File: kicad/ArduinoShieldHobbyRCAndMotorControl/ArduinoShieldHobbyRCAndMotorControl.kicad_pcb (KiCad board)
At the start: 2 copper layers, 68.6 x 53.3 mm, 18 parts, among them J1 Power, J2 Digital/PWM, J3 Analog, J4 Digital/PWM

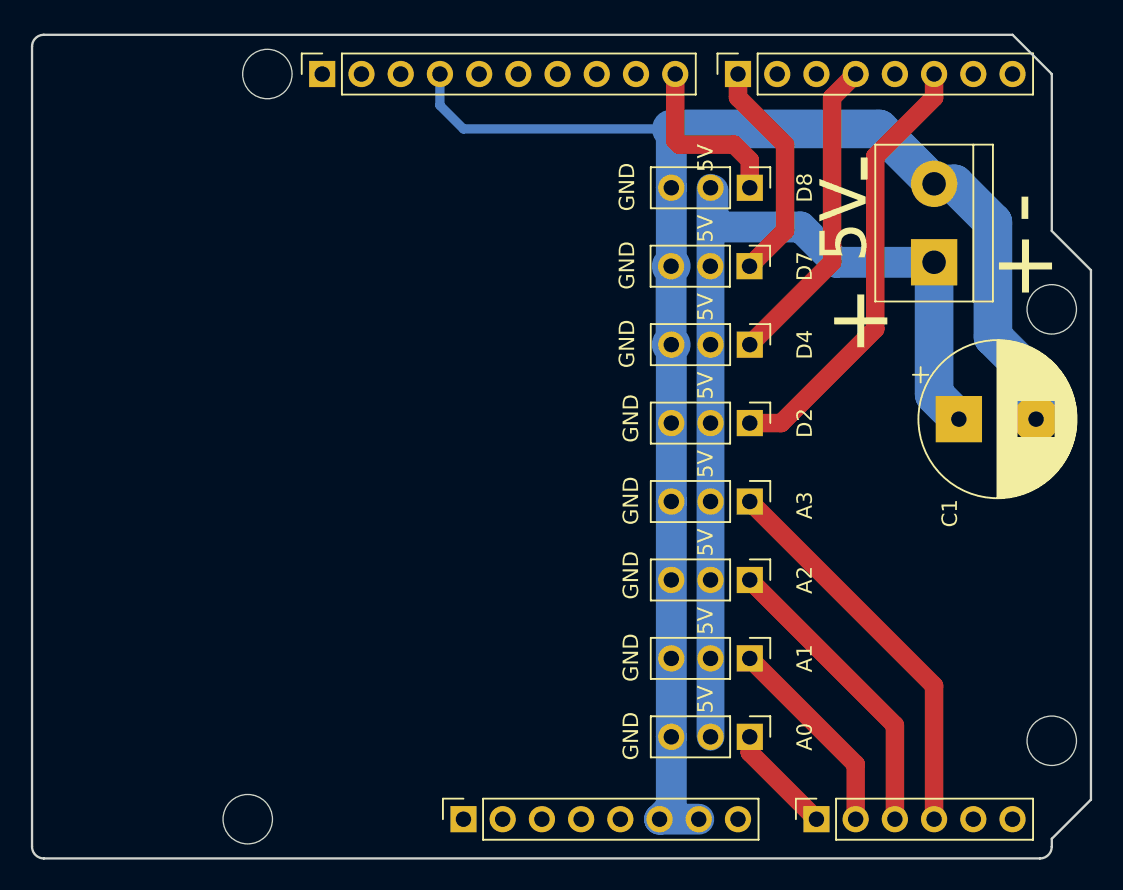
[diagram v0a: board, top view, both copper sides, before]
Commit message: finished hobby rc and motor controller shield
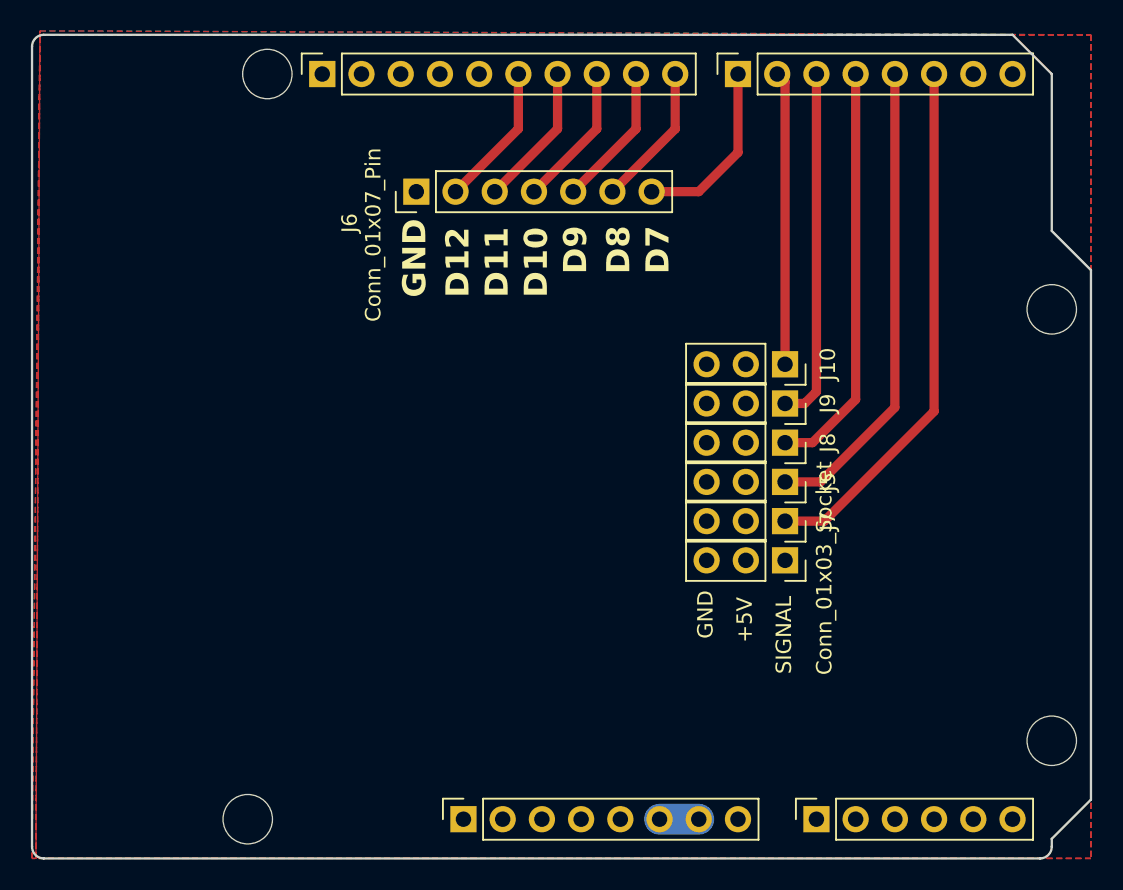
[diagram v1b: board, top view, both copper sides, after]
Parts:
- removed +__5V__-1: Screw_Terminal_01x02, TerminalBlock:TerminalBlock_bornier-2_P5.08mm
- removed A0, A1, A2, A3, D2, D4, D7, D8: Conn_01x03, Connector_PinHeader_2.54mm:PinHeader_1x03_P2.54mm_Vertical
- removed C1: 470 ufd, Capacitor_THT:CP_Radial_D10.0mm_P5.00mm
- added J10: Conn_01x03_Socket, Connector_PinSocket_2.54mm:PinSocket_1x03_P2.54mm_Vertical, F.Cu at (148.8, 68.0)
- added J11: Conn_01x03_Socket, Connector_PinSocket_2.54mm:PinSocket_1x03_P2.54mm_Vertical, F.Cu at (148.8, 80.7)
- added J5: Conn_01x03_Socket, Connector_PinSocket_2.54mm:PinSocket_1x03_P2.54mm_Vertical, F.Cu at (148.8, 75.6)
- added J6: Conn_01x07_Pin, Connector_PinHeader_2.54mm:PinHeader_1x07_P2.54mm_Vertical, F.Cu at (124.9, 56.8)
- added J7: Conn_01x03_Socket, Connector_PinSocket_2.54mm:PinSocket_1x03_P2.54mm_Vertical, F.Cu at (148.8, 78.2)
- added J8: Conn_01x03_Socket, Connector_PinSocket_2.54mm:PinSocket_1x03_P2.54mm_Vertical, F.Cu at (148.8, 73.1)
- added J9: Conn_01x03_Socket, Connector_PinSocket_2.54mm:PinSocket_1x03_P2.54mm_Vertical, F.Cu at (148.8, 70.5)
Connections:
- J1 pad 1: /AREF -> unconnected-(J1-Pin_1-Pad1)
- J2 pad 10: /8 -> Net-(J2-Pin_10)
- J2 pad 5: /13 -> unconnected-(J2-Pin_5-Pad5)
- J2 pad 6: /12 -> Net-(J2-Pin_6)
- J2 pad 7: /*11 -> Net-(J2-Pin_7)
- J2 pad 8: /*10 -> Net-(J2-Pin_8)
- J2 pad 9: /*9 -> Net-(J2-Pin_9)
- J3 pad 1: /A0 -> unconnected-(J3-Pin_1-Pad1)
- J3 pad 3: /A2 -> unconnected-(J3-Pin_3-Pad3)
- J3 pad 4: /A3 -> unconnected-(J3-Pin_4-Pad4)
- J4 pad 1: /7 -> Net-(J4-Pin_1)
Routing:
- net GND: track 102.5 -> 2.54 mm
- net Net-(+__5V__-1-Pin_1): track 64.0 -> 0.00 mm
- net /*3: track 0.00 -> 30.7 mm
- net /A3: track 25.5 -> 0.00 mm
- net /*5: track 0.00 -> 22.9 mm
- net /A2: track 19.4 -> 0.00 mm
- net /*6: track 0.00 -> 19.0 mm
- net /7: track 14.7 -> 0.00 mm
- net /A1: track 13.3 -> 0.00 mm
- net Net-(J4-Pin_1): track 0.00 -> 11.7 mm
- net /8: track 11.4 -> 0.00 mm
- net Net-(J2-Pin_10): track 0.00 -> 9.31 mm
- net Net-(J2-Pin_9): track 0.00 -> 9.31 mm
- net Net-(J2-Pin_6): track 0.00 -> 9.31 mm
- net Net-(J2-Pin_8): track 0.00 -> 9.31 mm
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- added copper zone on F.Cu, net +5V
- added copper zone on B.Cu, net GND
- added copper zone on F.Cu, net GND
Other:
- board text added: "+5V"
- board text added: "D10"
- board text added: "D11"
- board text added: "D12"
- board text added: "D7"
- board text added: "D8"
- board text added: "D9"
- board text added: "SIGNAL"
- board text removed: "+"
- board text removed: "-"
- board text removed: "5V"

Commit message: added DesignCyberneticsNavigatingTheNew.pdf and Table_of_Mechanicks_Cyclopaedia_Volume_2.jpg
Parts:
- removed J6: Conn_01x07_Pin, Connector_PinHeader_2.54mm:PinHeader_1x07_P2.54mm_Vertical
- added REF**: TerminalBlock_WAGO_236-107_1x07_P5.00mm_45Degree, TerminalBlock_WAGO:TerminalBlock_WAGO_236-107_1x07_P5.00mm_45Degree, F.Cu at (115.5, 58.0)
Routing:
- net Net-(J4-Pin_1): track 11.7 -> 0.00 mm
- removed copper zone on B.Cu, net GND
- removed copper zone on F.Cu, net GND
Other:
- board text added: "D2"
- board text added: "D3"
- board text added: "D4"
- board text added: "D5"
- board text added: "D6"

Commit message: rev 2 of arduino shield hobby rc and motor control
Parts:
- removed REF**: TerminalBlock_WAGO_236-107_1x07_P5.00mm_45Degree, TerminalBlock_WAGO:TerminalBlock_WAGO_236-107_1x07_P5.00mm_45Degree
- added J6: Conn_01x07_Pin, TerminalBlock_WAGO:TerminalBlock_WAGO_236-107_1x07_P5.00mm_45Degree, F.Cu at (115.5, 58.5)
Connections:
- J2 pad 1: /SCL/A5 -> unconnected-(J2-Pin_1-Pad1)
- J2 pad 2: /SDA/A4 -> unconnected-(J2-Pin_2-Pad2)
- J3 pad 2: /A1 -> unconnected-(J3-Pin_2-Pad2)
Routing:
- net Net-(J4-Pin_1): track 0.00 -> 9.39 mm
- net Net-(J2-Pin_6): track 9.31 -> 15.7 mm
- net Net-(J2-Pin_7): track 9.31 -> 12.8 mm
- net Net-(J2-Pin_8): track 9.31 -> 12.0 mm
- net Net-(J2-Pin_9): track 9.31 -> 10.8 mm
- added copper zone on B.Cu, net +5V
- added copper zone on F.Cu, net GND
